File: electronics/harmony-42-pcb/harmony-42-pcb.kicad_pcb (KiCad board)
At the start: 2 copper layers, 285.8 x 133.3 mm, 84 parts

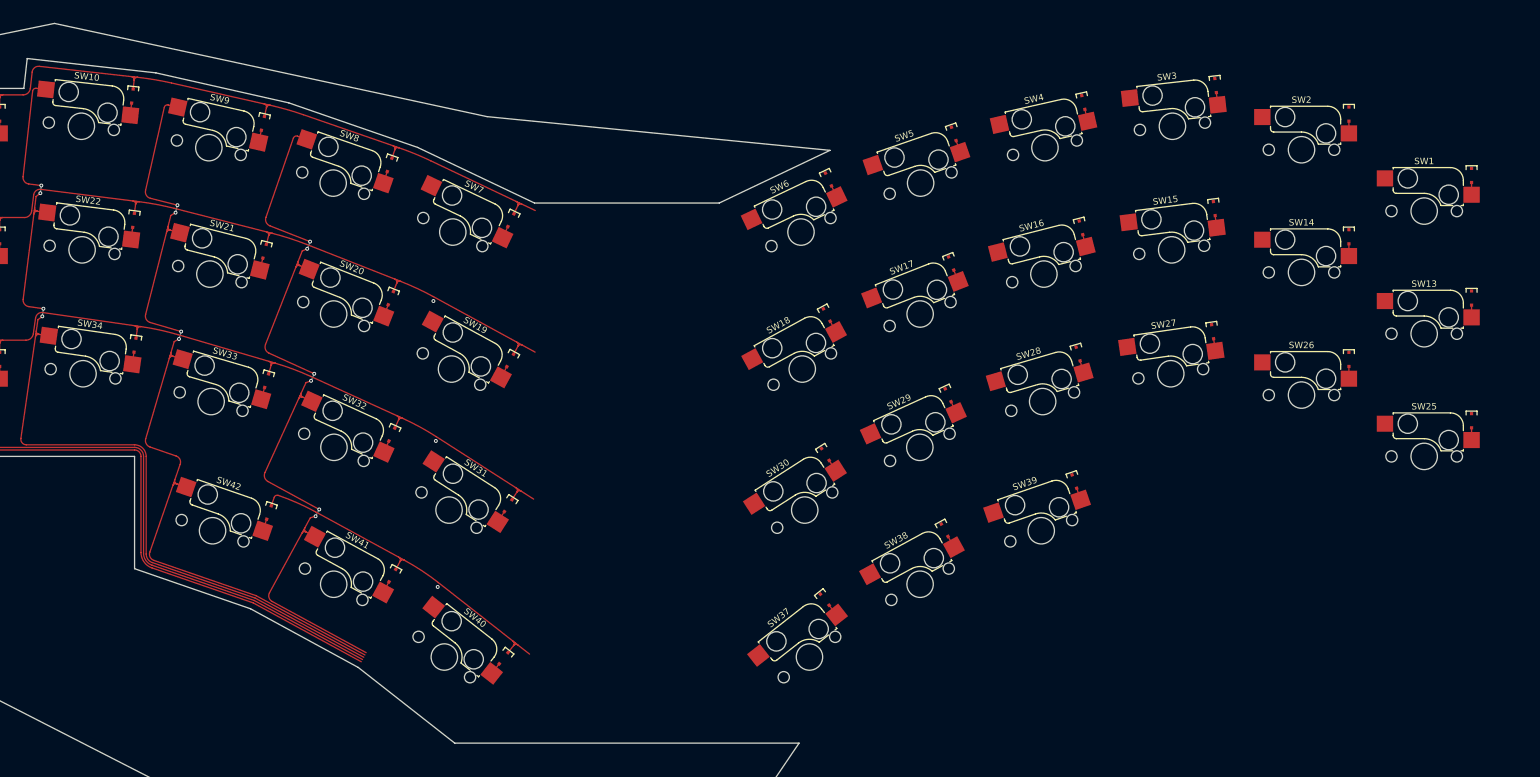
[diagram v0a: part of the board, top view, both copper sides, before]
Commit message: Add routes for one side
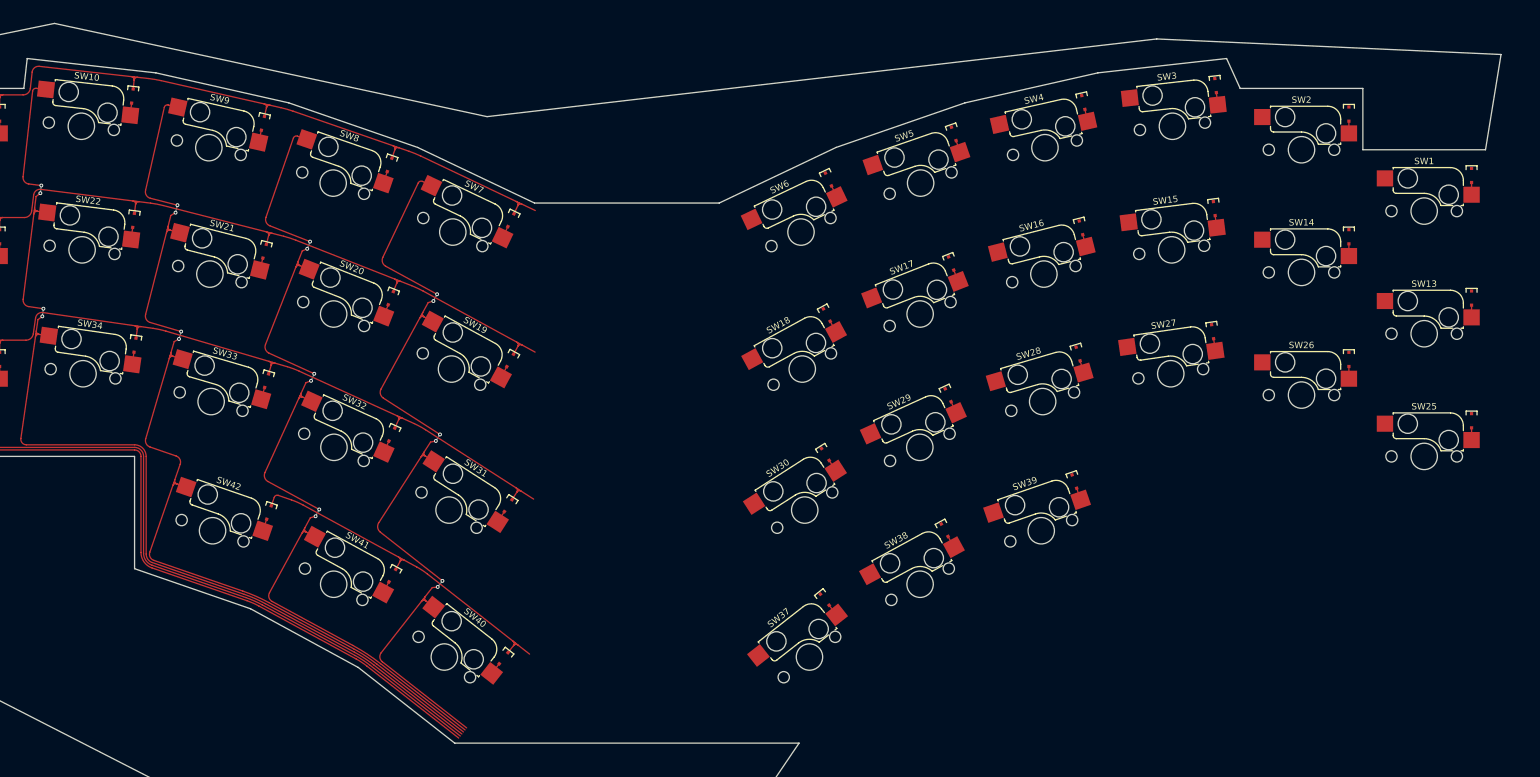
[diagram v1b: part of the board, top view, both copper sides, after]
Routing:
- net Net-(SW19-Pad1): track 0.00 -> 3.60 mm, vias 0 -> 6
- net Net-(SW11-Pad1): vias 5 -> 4
- net Net-(D37-K): vias 1 -> 0
- net Net-(D25-K): vias 1 -> 0
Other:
- outline, holes or cut-outs redrawn
